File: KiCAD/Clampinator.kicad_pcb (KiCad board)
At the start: 4 copper layers, 200 x 115 mm, 196 parts, among them J1 Power, J10 Conn_01x04, J11 Conn_01x04, J12 FDCAN_1, J13 FDCAN_2, J14 10k NTC, J15 10k NTC, J16 EN_NTC_B, J17 EN_NTC_A, J18 FAN, J19 FAN, J20 VP0265840000G, J23 VP0265840000G, J24 VP0265840000G, J25 +5V INJ, J5 Debug Header, J6 Conn_01x04, J7 Conn_01x04, J8 Conn_01x04, J9 Conn_01x04, Q1 TK100E10N1,S1X, Q10 AO3400A, Q2 TK100E10N1,S1X, Q3 TK100E10N1,S1X, Q4 TK100E10N1,S1X, Q5 TK100E10N1,S1X, Q6 AO3400A, Q7 AO3400A, Q8 AO3400A, Q9 MMBT3904-C20526, SW1 PTS810SJM250SMTRLFS, SW2 PTS810SJM250SMTRLFS, SW3 PTS810SJM250SMTRLFS, SW4 PTS810SJM250SMTRLFS, SW5 SMQS-02R-TP, SW6 EG1847-ND, SW7 GPI-154-3013, U1 STM32H573RIT6, U10 LM74810QDRRRQ1, U12 TPS7A2033DQNR, U13 VOS618A-3T, U14 LM5163DDAR, U2 TL432BQDBZR, U3 EG2131, U4 UCC33420RAQR_C46461551, U5 USBLC6-2SC6, U6 LM5012DDAR, U7 MCP2562FD-E/P, U8 MCP2562FD-E/P, U9 EL357N, X1 SC-32S32.768kHz20PPM7pF, Y2 ECS-80-18-23B-JTM-TR

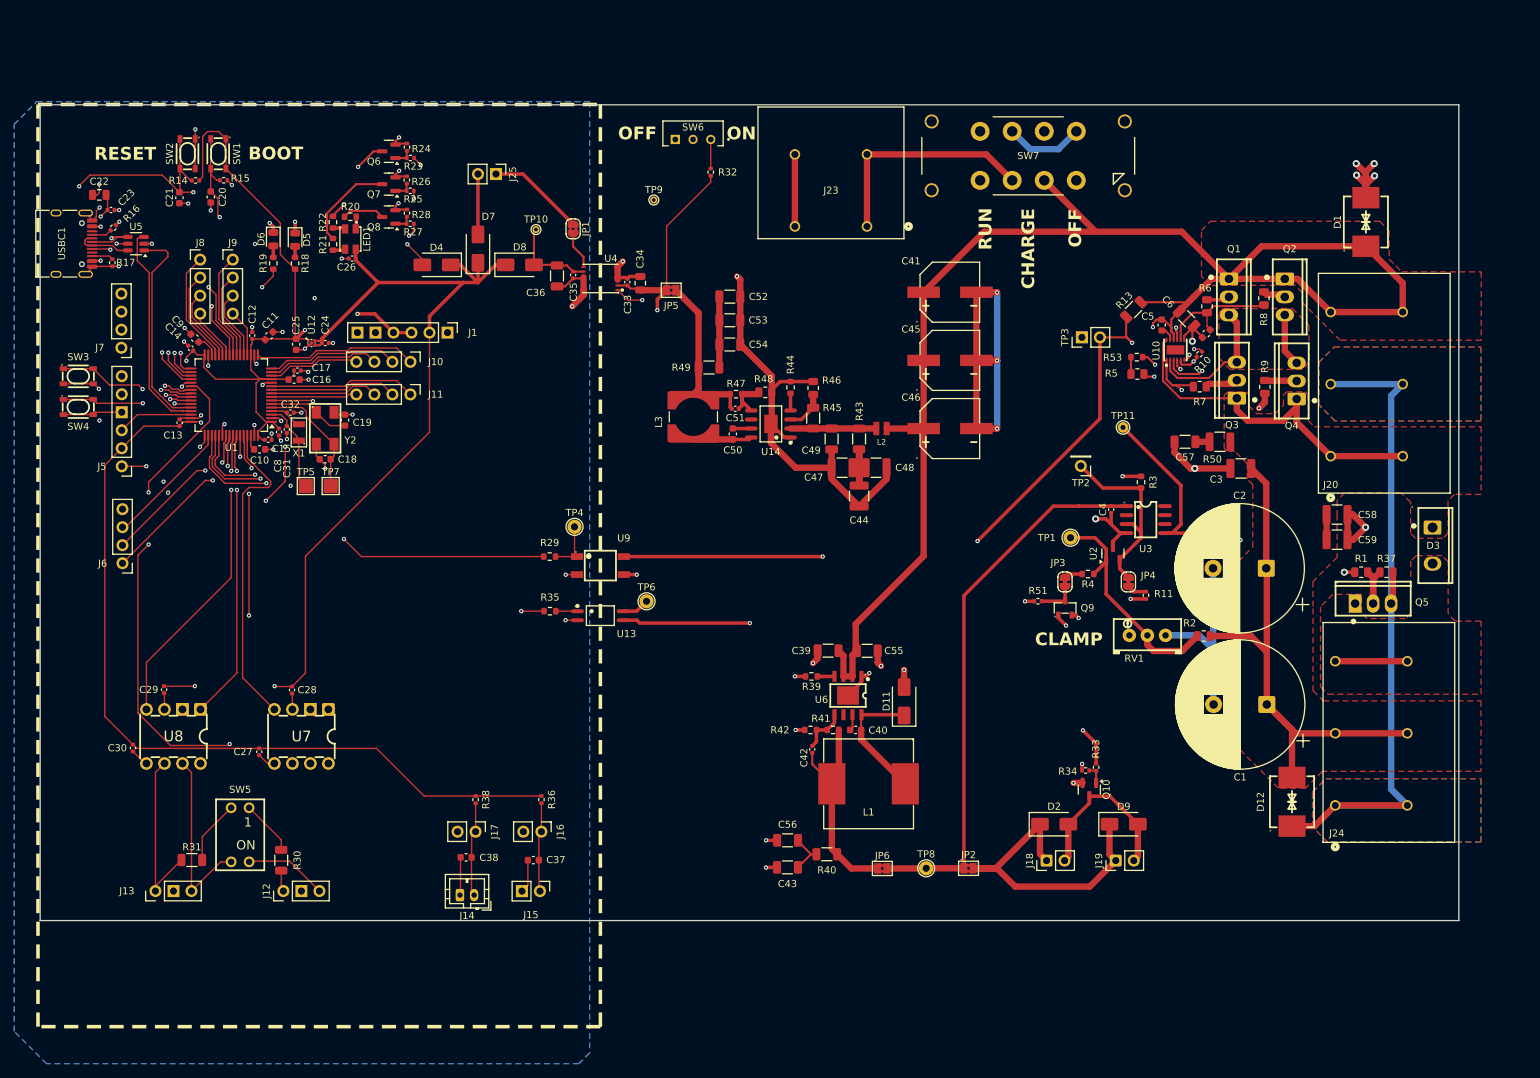
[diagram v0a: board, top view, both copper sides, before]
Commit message: L3 and L4 Power GND Keep Outs, Shifting Footprints
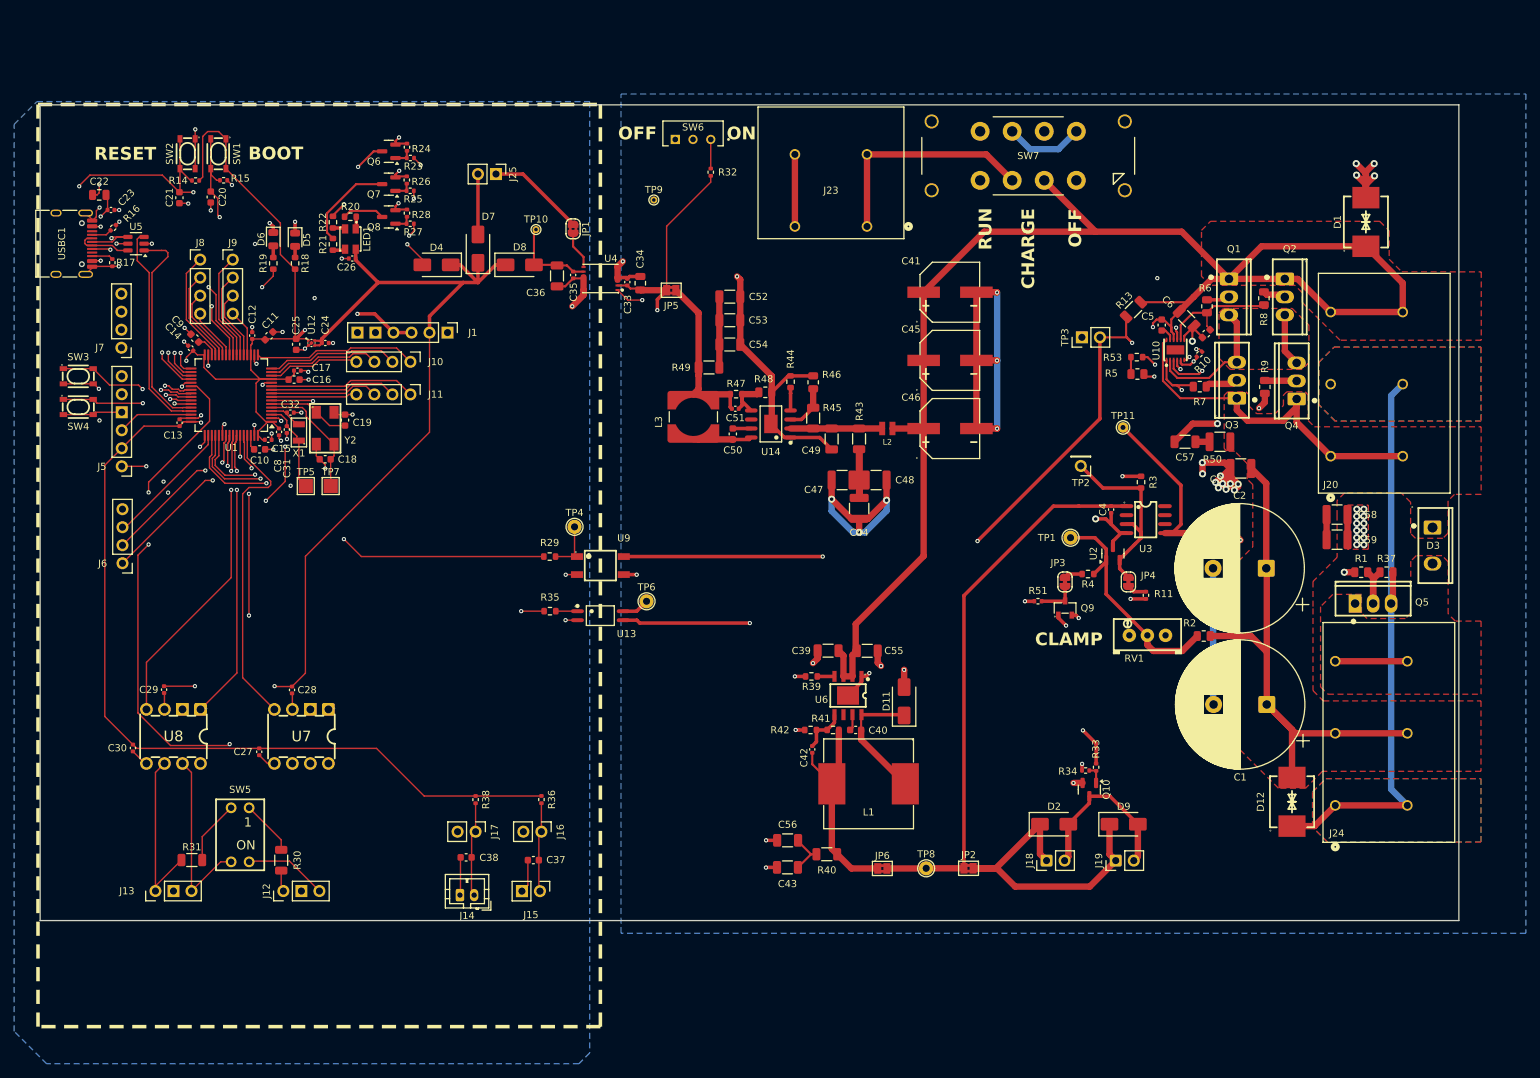
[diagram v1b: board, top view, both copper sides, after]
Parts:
- moved C47 1.74 mm to (160.9, 77.4)
- moved C48 1.74 mm to (165.7, 77.4)
- moved C44 1.74 mm to (163.3, 81.4)
- moved L2 0.82 mm to (167.2, 70.2)
- moved R44 0.80 mm to (153.6, 63.6)
- moved R46 0.80 mm to (156.8, 63.6)
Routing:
- net DC_GND: track 334.0 -> 345.0 mm, vias 26 -> 51
- net Net-(C44-Pad1): track 16.9 -> 22.1 mm
- net Net-(U14-VIN): track 12.1 -> 12.9 mm
- net DC_VIN: track 258.2 -> 257.4 mm
- net Net-(U14-RON): track 2.43 -> 3.23 mm
- net Net-(U14-EN/UVLO): track 5.75 -> 6.55 mm

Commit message: Add M3 mounting holes, Fix DRC Errors, Merge L3 Quiet Power GND Fills
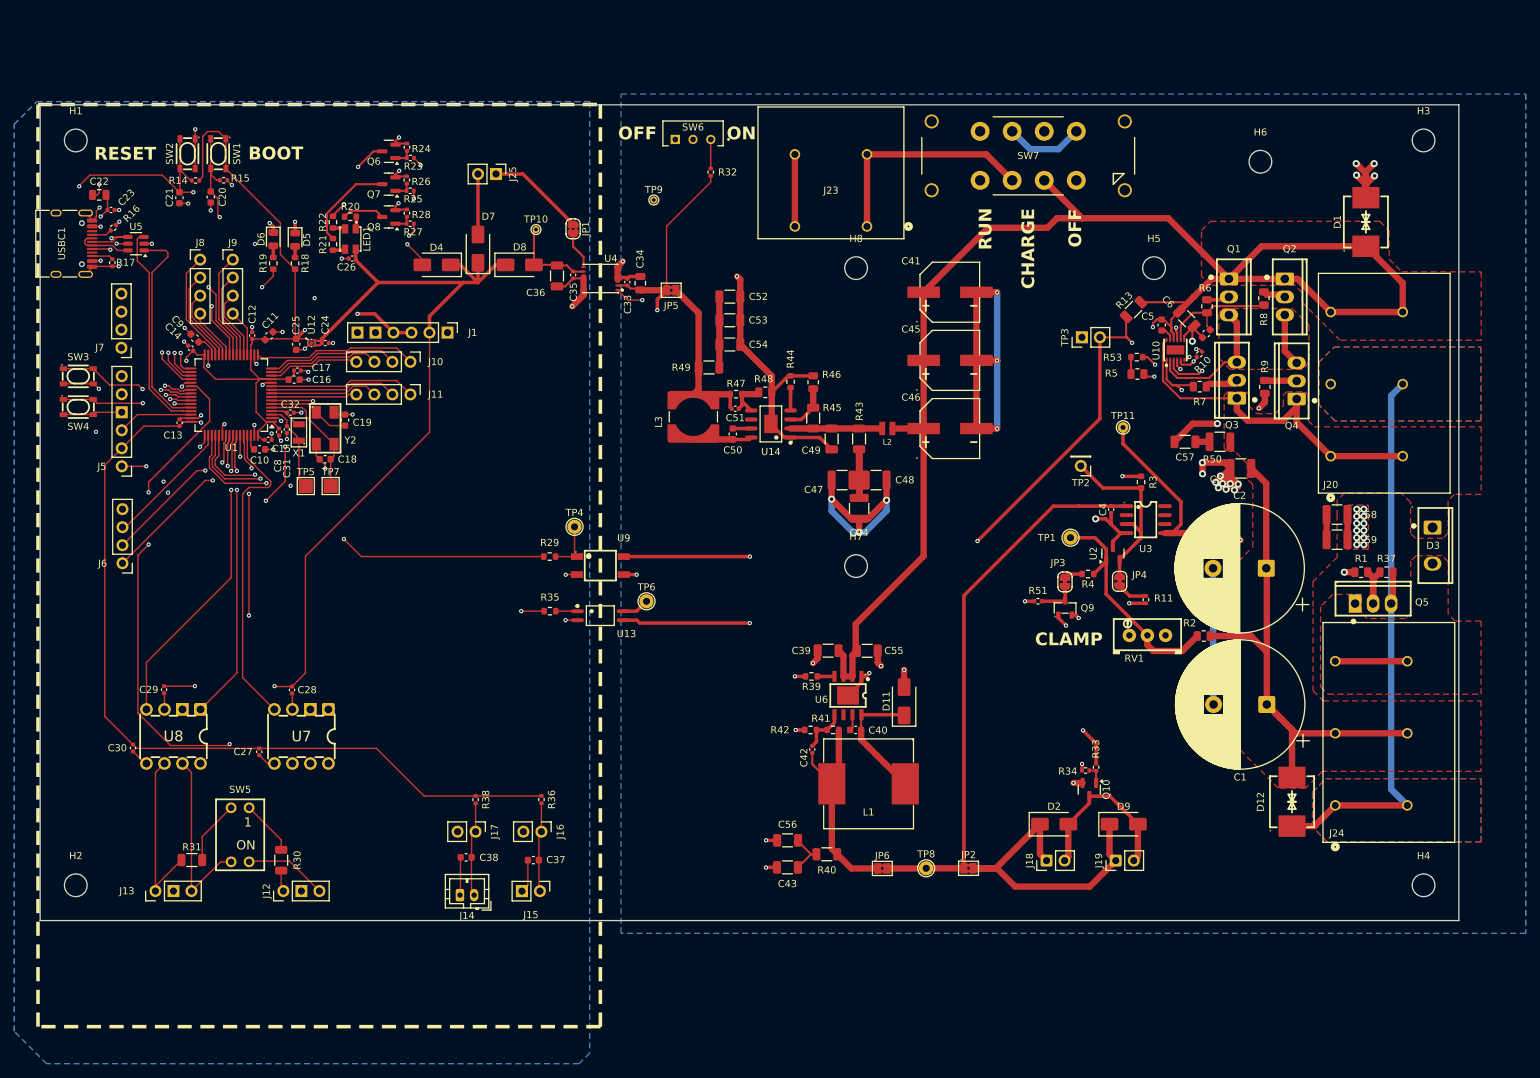
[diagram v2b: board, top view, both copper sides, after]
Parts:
- added H1: MountingHole, MountingHole:MountingHole_3.2mm_M3, F.Cu at (52.8, 29.6)
- added H2: MountingHole, MountingHole:MountingHole_3.2mm_M3, F.Cu at (52.8, 134.6)
- added H3: MountingHole, MountingHole:MountingHole_3.2mm_M3, F.Cu at (242.8, 29.6)
- added H4: MountingHole, MountingHole:MountingHole_3.2mm_M3, F.Cu at (242.8, 134.6)
- added H5: MountingHole, MountingHole:MountingHole_3.2mm_M3, F.Cu at (204.8, 47.6)
- added H6: MountingHole, MountingHole:MountingHole_3.2mm_M3, F.Cu at (219.8, 32.6)
- added H7: MountingHole, MountingHole:MountingHole_3.2mm_M3, F.Cu at (162.8, 89.6)
- added H8: MountingHole, MountingHole:MountingHole_3.2mm_M3, F.Cu at (162.8, 47.6)
- moved JP4 1.24 mm to (200.0, 91.7)
- moved R11 0.62 mm to (203.7, 94.3)
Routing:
- net DC_GND: track 345.0 -> 333.5 mm, vias 51 -> 50
- net EN_DIODE: track 143.0 -> 147.3 mm
- net BRAKE_A: track 371.8 -> 375.7 mm
- net Net-(JP4-B): track 2.77 -> 4.30 mm
- net DC_VIN: track 257.4 -> 256.3 mm
- net Net-(JP4-A): track 27.5 -> 26.9 mm

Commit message: Change some TPs to 2.54mm pin headers, silkscreen changes, start led redo
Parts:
- TP11: footprint TestPoint:TestPoint_THTPad_D1.5mm_Drill0.7mm -> Connector_PinHeader_2.54mm:PinHeader_1x01_P2.54mm_Vertical
- moved TP11 10.2 mm to (206.7, 78.1)
- moved TP4 6.55 mm to (117.4, 80.8)
- moved SW4 0.40 mm to (53.2, 67.5)
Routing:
- net DC_GND: track 333.5 -> 298.2 mm, vias 50 -> 54
- net Net-(U3-LO): track 48.9 -> 38.2 mm
- net Net-(U9-AN): track 7.35 -> 14.7 mm
- net CAN1_STBY: track 81.8 -> 82.5 mm
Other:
- board text added: "1"
- board text added: "10k NTC"
- board text added: "2"
- board text added: "3"
- board text added: "4"
- board text added: "A"
- board text added: "B"
- board text added: "EN"
- board text added: "PA8"
- board text added: "PA9"
- board text added: "USB-C"

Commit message: Replace RGB LED with cheaper SK6812 LEDs, expose freed UART pins
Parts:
- removed LED1: HL-AF-3528S39FU70GH203BC-A-S1-HL, easyeda2kicad:LED-SMD_4P-L3.2-W2.7-TL_HL-AF-3528S39FU70GH20
- removed Q6, Q7, Q8: AO3400A, Package_TO_SOT_SMD:SOT-23
- removed R20, R21: 200R, Resistor_SMD:R_0603_1608Metric
- removed R22: 120R, Resistor_SMD:R_0603_1608Metric
- removed R23, R25, R27: 220R, Resistor_SMD:R_0402_1005Metric
- removed R24, R26, R28: 10k, Resistor_SMD:R_0402_1005Metric
- added D10: SK6812MINI-E, LED_SMD:LED_SK6812MINI-E_3.2x2.8mm_P1.5mm_ReverseMount, F.Cu at (92.7, 15.4)
- added D13: SS34, Diode_SMD:D_SMA, F.Cu at (101.0, 27.4)
- added D14: SK6812MINI-E, LED_SMD:LED_SK6812MINI-E_3.2x2.8mm_P1.5mm_ReverseMount, F.Cu at (92.7, 20.3)
- added D15: SK6812MINI-E, LED_SMD:LED_SK6812MINI-E_3.2x2.8mm_P1.5mm_ReverseMount, F.Cu at (92.7, 25.1)
- added D16: SK6812MINI-E, LED_SMD:LED_SK6812MINI-E_3.2x2.8mm_P1.5mm_ReverseMount, F.Cu at (92.7, 30.0)
- added J26: UART4, Connector_PinHeader_2.54mm:PinHeader_1x04_P2.54mm_Vertical, F.Cu at (100.2, 73.1)
- moved J10 0.97 mm to (100.2, 61.7)
- moved J11 0.23 mm to (100.2, 65.5)
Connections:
- U1 pad 51: PC10_RED -> PC10_TX
- U1 pad 52: PC11_GREEN -> PC11_RX
- U1 pad 53: PC12_BLUE -> PC12_RGB_DIN
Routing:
- net PC12_RGB_DIN: track 0.00 -> 65.4 mm, vias 0 -> 2
- net PC12_BLUE: track 65.4 -> 0.00 mm, vias 2 -> 0
- net PC11_RX: track 0.00 -> 61.6 mm, vias 0 -> 2
- net PC11_GREEN: track 61.6 -> 0.00 mm, vias 2 -> 0
- net PC10_TX: track 0.00 -> 58.8 mm, vias 0 -> 2
- net PC10_RED: track 58.8 -> 0.00 mm, vias 2 -> 0
- net Net-(Q7-D): track 13.4 -> 0.00 mm
- net Net-(Q6-D): track 12.7 -> 0.00 mm, vias 2 -> 0
- net GND: track 115.7 -> 107.2 mm, vias 40 -> 37
- net Net-(Q8-D): track 6.00 -> 0.00 mm
- net +5VS: track 131.8 -> 137.0 mm
- net Net-(Q6-G): track 2.63 -> 0.00 mm
- net Net-(Q7-G): track 2.60 -> 0.00 mm
- net Net-(Q8-G): track 2.59 -> 0.00 mm
- net Net-(LED1-G): track 1.77 -> 0.00 mm
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
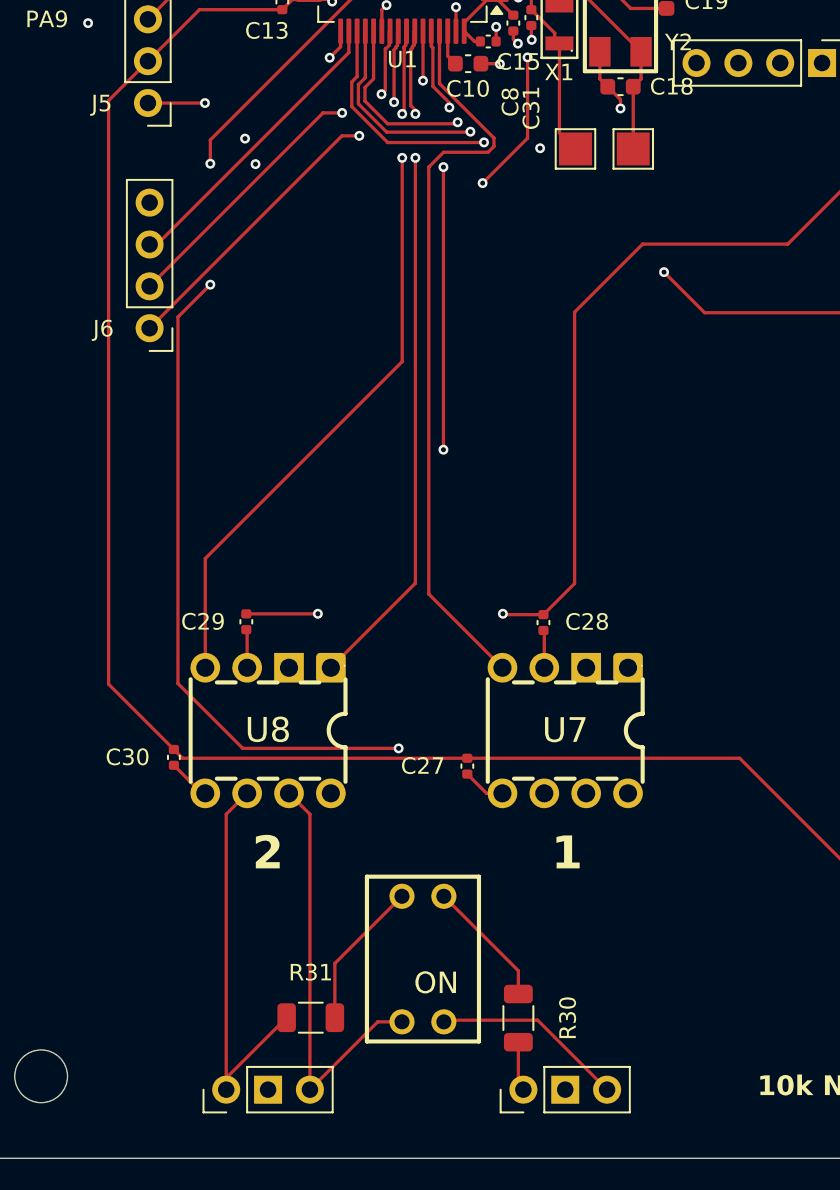
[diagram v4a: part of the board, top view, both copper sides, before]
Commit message: Fixed silly miswired CAN transceivers
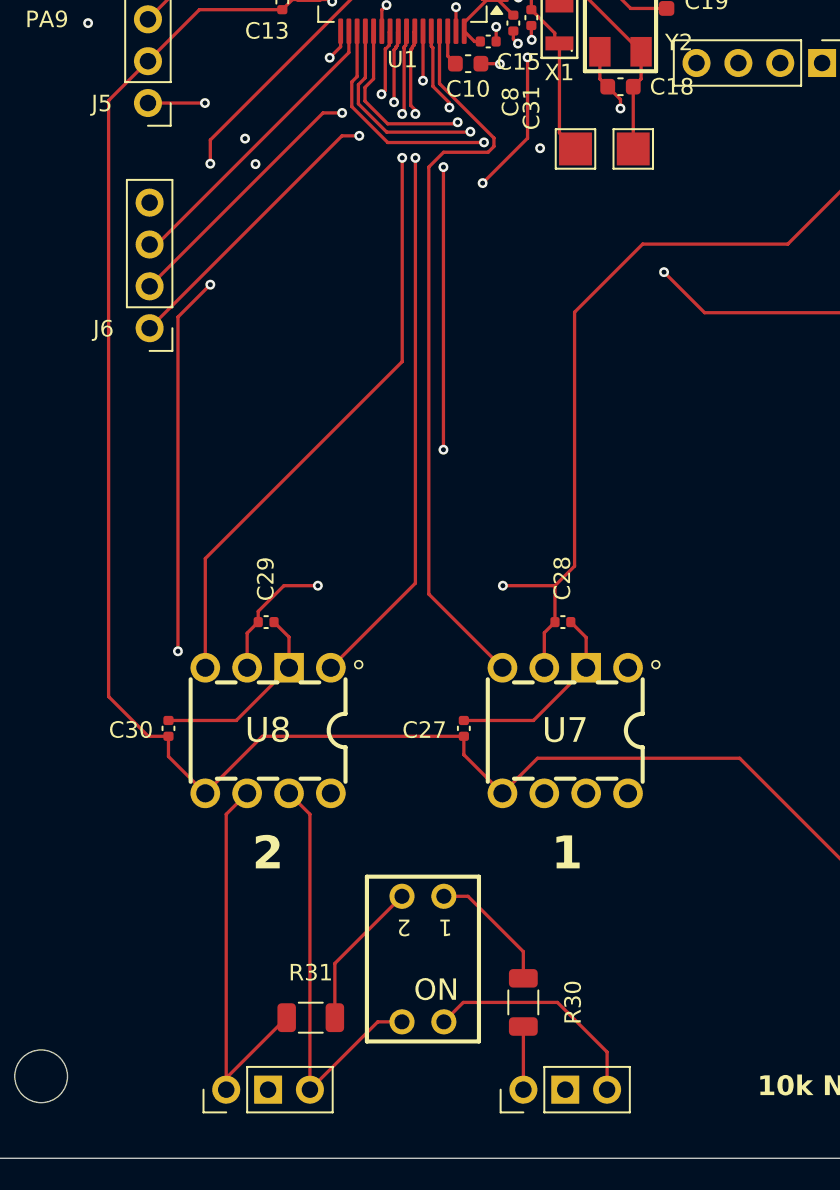
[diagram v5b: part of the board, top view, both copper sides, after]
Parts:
- moved C27 2.30 mm to (78.5, 113.4), turned to 90 degrees
- moved C30 1.79 mm to (60.6, 113.4), turned to 90 degrees
- moved C29 1.20 mm to (66.5, 107.0), turned to 180 degrees
- moved C28 1.18 mm to (84.5, 107.0), turned to 0 degrees
- moved R30 1.00 mm to (82.1, 130.1)
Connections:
- C27 pad 2: Net-(U7-VIO) -> GND
- C28 pad 2: Net-(U7-VDD) -> GND
- C29 pad 1: +5VS -> GND
- C29 pad 2: Net-(U8-VDD) -> +5VS
- C30 pad 2: Net-(U8-VIO) -> GND
- U7 pad 3: Net-(U7-VDD) -> +5VS
- U7 pad 5: Net-(U7-VIO) -> +3V3
- U8 pad 3: Net-(U8-VDD) -> +5VS
- U8 pad 5: Net-(U8-VIO) -> +3V3
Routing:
- net GND: track 107.2 -> 130.9 mm
- net +5VS: track 137.0 -> 144.5 mm
- net +3V3: track 238.0 -> 244.6 mm
- net Net-(U7-VIO): track 2.62 -> 0.00 mm
- net Net-(U8-VIO): track 2.61 -> 0.00 mm
- net Net-(U8-VDD): track 2.33 -> 0.00 mm
- net Net-(U7-VDD): track 2.28 -> 0.00 mm
- net CANH_1: track 30.2 -> 32.4 mm
- net CANL_1: track 21.5 -> 22.3 mm
